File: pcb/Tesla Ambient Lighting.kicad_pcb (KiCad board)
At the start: 2 copper layers, 56.5 x 50.2 mm, 24 parts, among them J1 LED_1, J2 LED_2, J3 LED_3, J4 LED_4, J5 CHASSIS_CAN, J6 USB4105-GF-A, J7 Screw_Terminal_01x02, SW1 BOOT_OPTION, U1 ESP32-WROOM-32, U2 SN65HVD230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

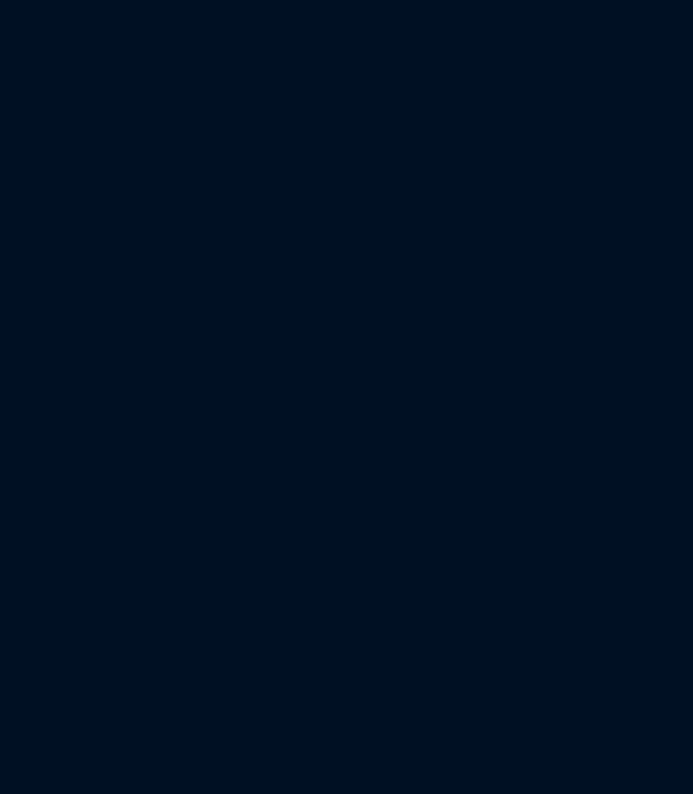
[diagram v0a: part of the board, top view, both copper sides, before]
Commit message: started PCB V2; adding DTR and RTS control pins, RST button, and power LED; also wanting to add serial LED
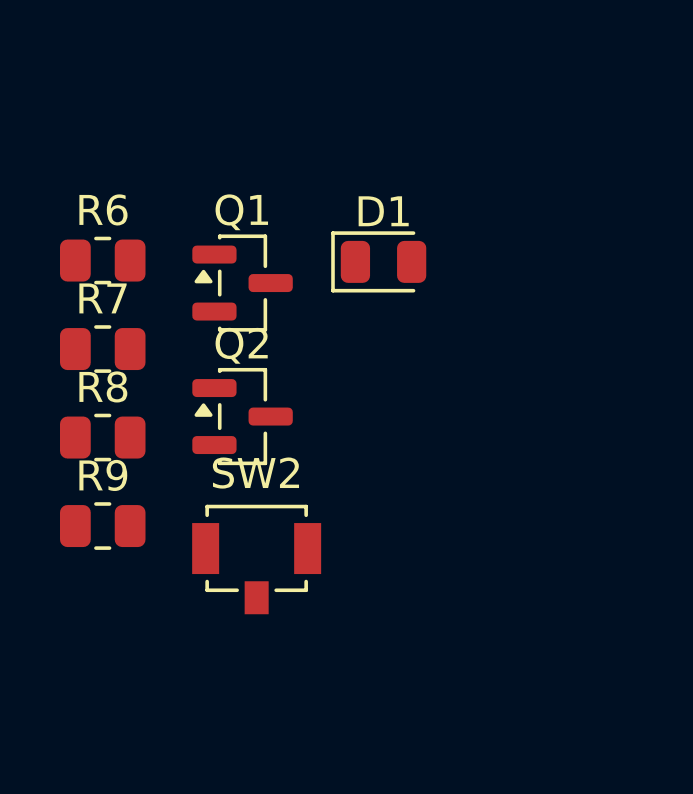
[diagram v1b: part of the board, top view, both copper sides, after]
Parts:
- added D1: PWR_LED, LED_SMD:LED_0805_2012Metric, F.Cu at (105.5, 88.9)
- added Q1: Q_NPN_BEC, Package_TO_SOT_SMD:SOT-23, F.Cu at (100.8, 89.7)
- added Q2: Q_NPN_BEC, Package_TO_SOT_SMD:SOT-23, F.Cu at (100.8, 94.1)
- added R6: 50, Resistor_SMD:R_0805_2012Metric, F.Cu at (96.2, 88.9)
- added R7: 10k, Resistor_SMD:R_0805_2012Metric, F.Cu at (96.2, 91.8)
- added R8: 10k, Resistor_SMD:R_0805_2012Metric, F.Cu at (96.2, 94.8)
- added R9: 10k, Resistor_SMD:R_0805_2012Metric, F.Cu at (96.2, 97.8)
- added SW2: RESET, Button_Switch_SMD:SW_SPST_B3U-1100P, F.Cu at (101.3, 99.3)
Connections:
- net Net-(U1-EN) renamed /EN
- net Net-(U1-IO0) renamed /GPIO0
- SW1 pad 3: GNDREF -> (no net)
- U5 pad 1: unconnected-(U5-~{DTR}-Pad1) -> GNDREF
- U5 pad 2: unconnected-(U5-~{RTS}-Pad2) -> /RTS

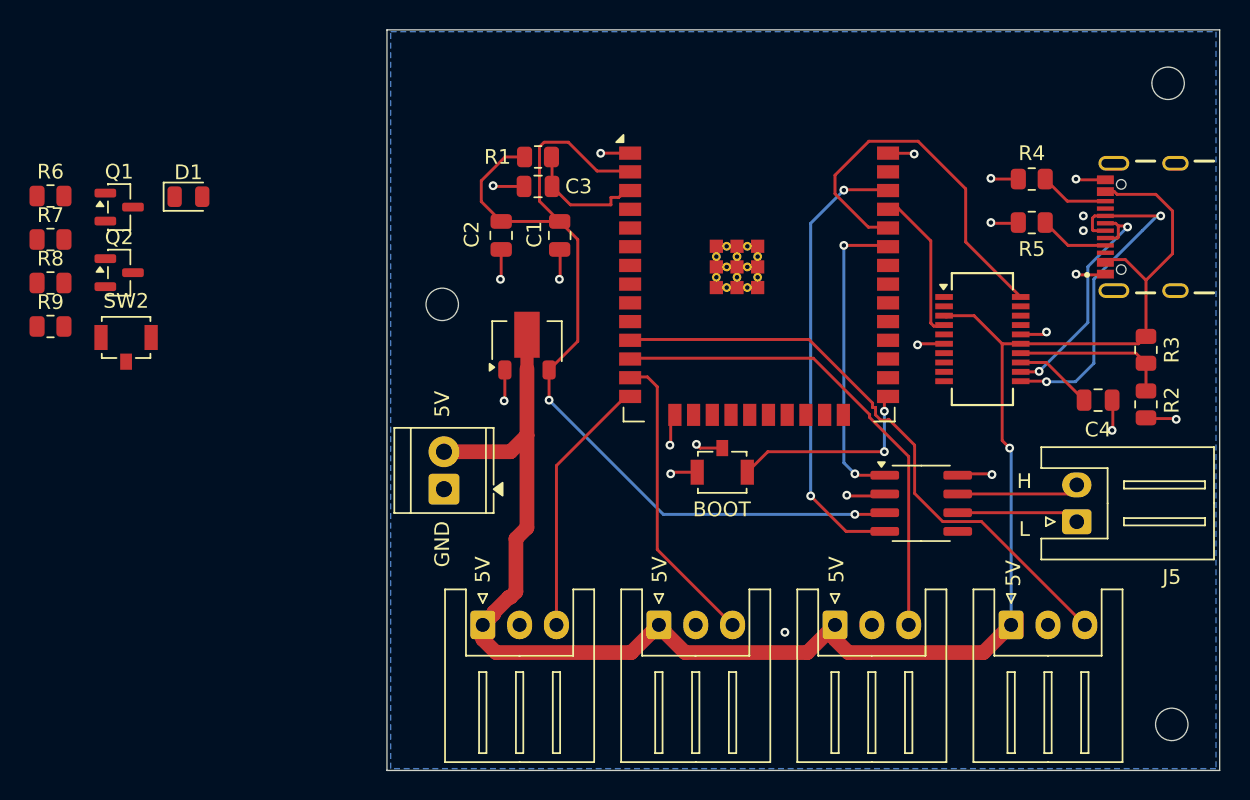
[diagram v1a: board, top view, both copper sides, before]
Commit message: updated pcb to have RST button, power LED, and flow control
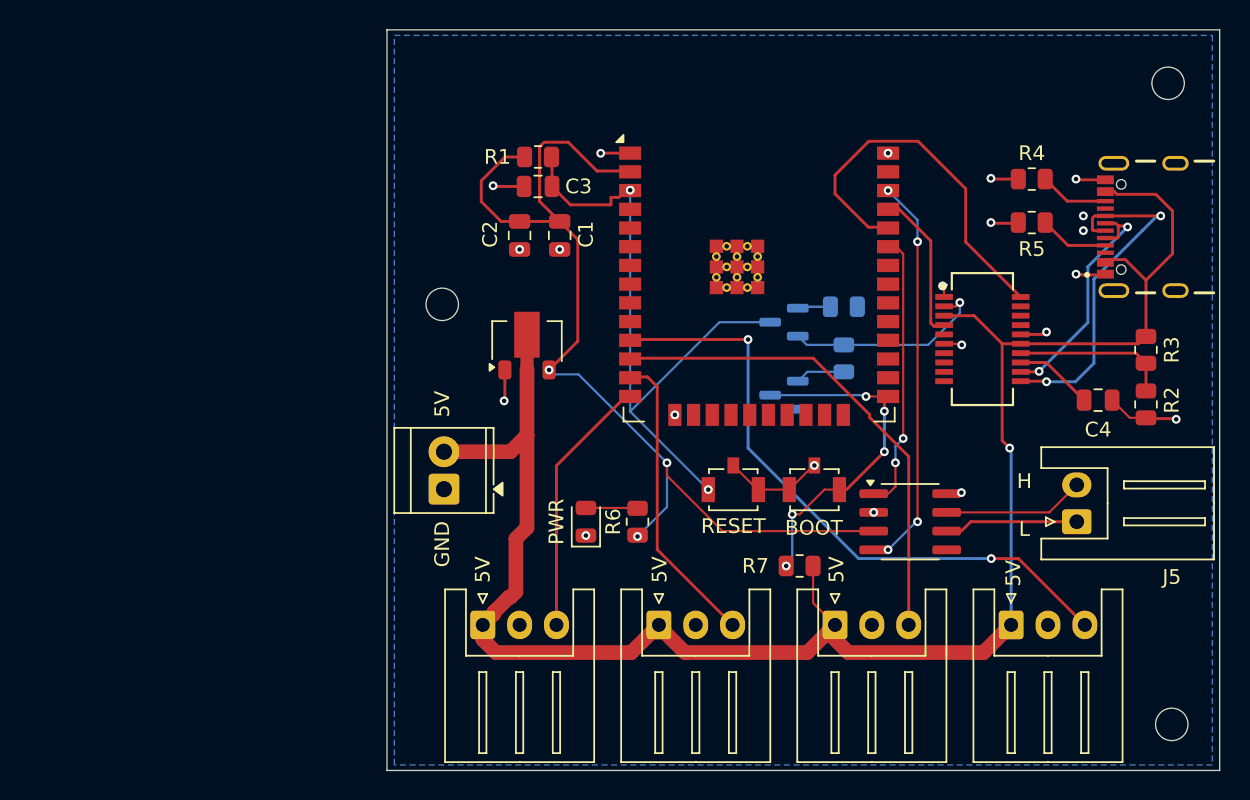
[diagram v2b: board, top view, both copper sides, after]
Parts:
- Q1, Q2, R8, R9: moved to B.Cu
- moved R7 55.4 mm to (147.0, 114.0), turned to 180 degrees
- moved R9 53.9 mm to (150.0, 99.9), turned to -90 degrees
- moved R8 53.9 mm to (150.0, 96.4), turned to 180 degrees
- moved Q2 45.9 mm to (145.9, 102.4), turned to 180 degrees
- moved Q1 45.8 mm to (145.9, 97.5), turned to 180 degrees
- moved R6 45.6 mm to (136.0, 111.0), turned to 90 degrees
- moved RESET 42.1 mm to (142.5, 108.0), turned to 180 degrees
- moved PWR 34.8 mm to (132.5, 111.0), turned to 90 degrees
- moved SW1 6.36 mm to (148.0, 108.0)
- moved U2 1.46 mm to (154.5, 111.0)
- moved C2 1.25 mm to (128.0, 91.6)
- renumbered D1 to PWR, SW2 to RESET
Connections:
- RESET pad 3: (no net) -> GNDREF
- SW1 pad 3: (no net) -> GNDREF
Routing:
- net /EN: track 8.30 -> 42.8 mm, vias 0 -> 2
- net /RTS: track 0.00 -> 13.5 mm, vias 0 -> 1
- net /GPIO0: track 13.7 -> 23.5 mm, vias 2 -> 5
- net GNDREF: track 36.7 -> 29.3 mm
- net /V33: track 62.8 -> 67.9 mm, vias 2 -> 3
- net /V5: track 118.5 -> 123.1 mm
- net /CAN_RXD: track 30.5 -> 26.1 mm, vias 2 -> 4
- net Net-(D1-A): track 0.00 -> 3.56 mm
- net Net-(Q2-B): track 0.00 -> 2.89 mm
- net /CAN_TXD: track 20.6 -> 17.9 mm
- net Net-(Q1-B): track 0.00 -> 2.40 mm
- net Net-(J4-Pin_3): track 41.6 -> 43.5 mm, vias 0 -> 2
- net Net-(J5-Pin_2): track 8.33 -> 9.47 mm
- net Net-(J5-Pin_1): track 8.33 -> 8.96 mm
- net (no net): vias 3 -> 2
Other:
- board text added: "jaketheduque - v2"
